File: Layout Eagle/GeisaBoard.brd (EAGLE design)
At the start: 100 x 80 mm, 20 parts, among them IC1 4052N, IC2 4052N, U1 328P

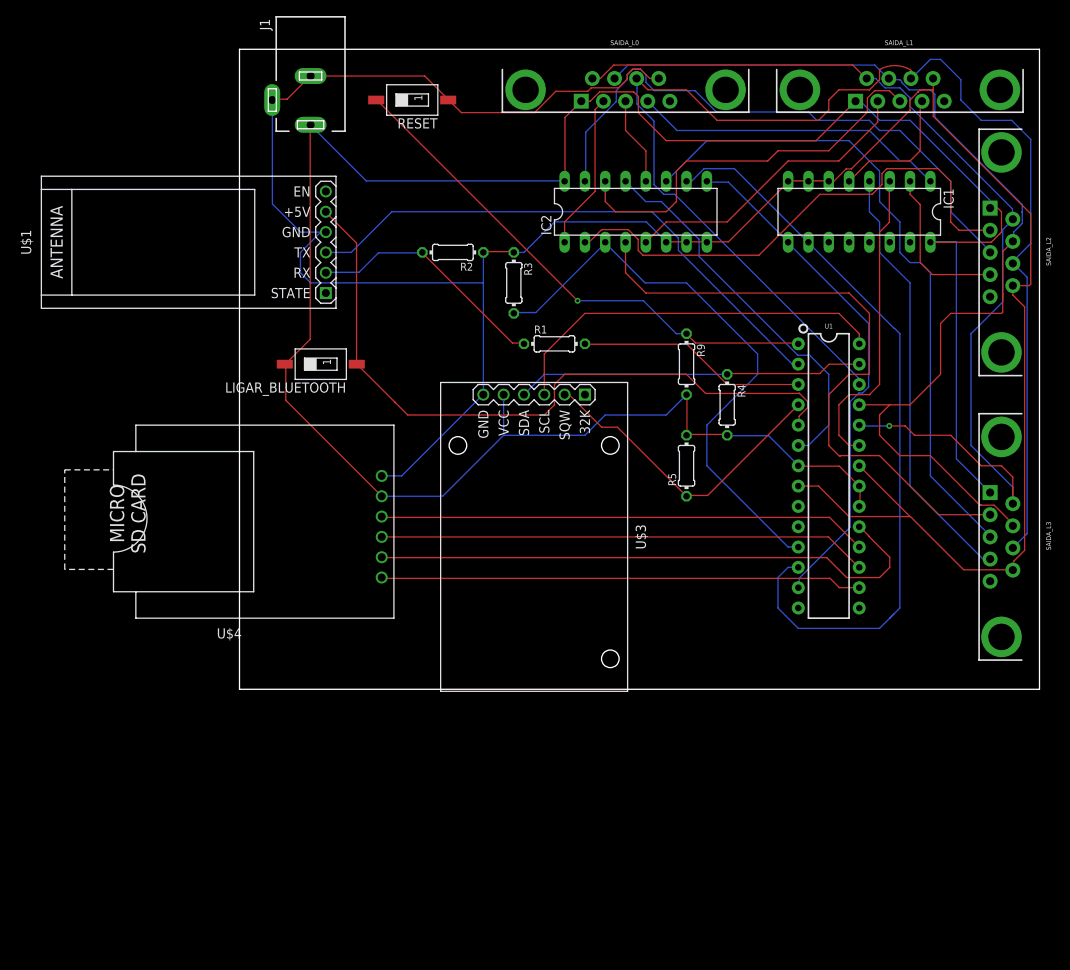
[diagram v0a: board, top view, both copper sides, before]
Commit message: Layout com correção inicial do Padrão
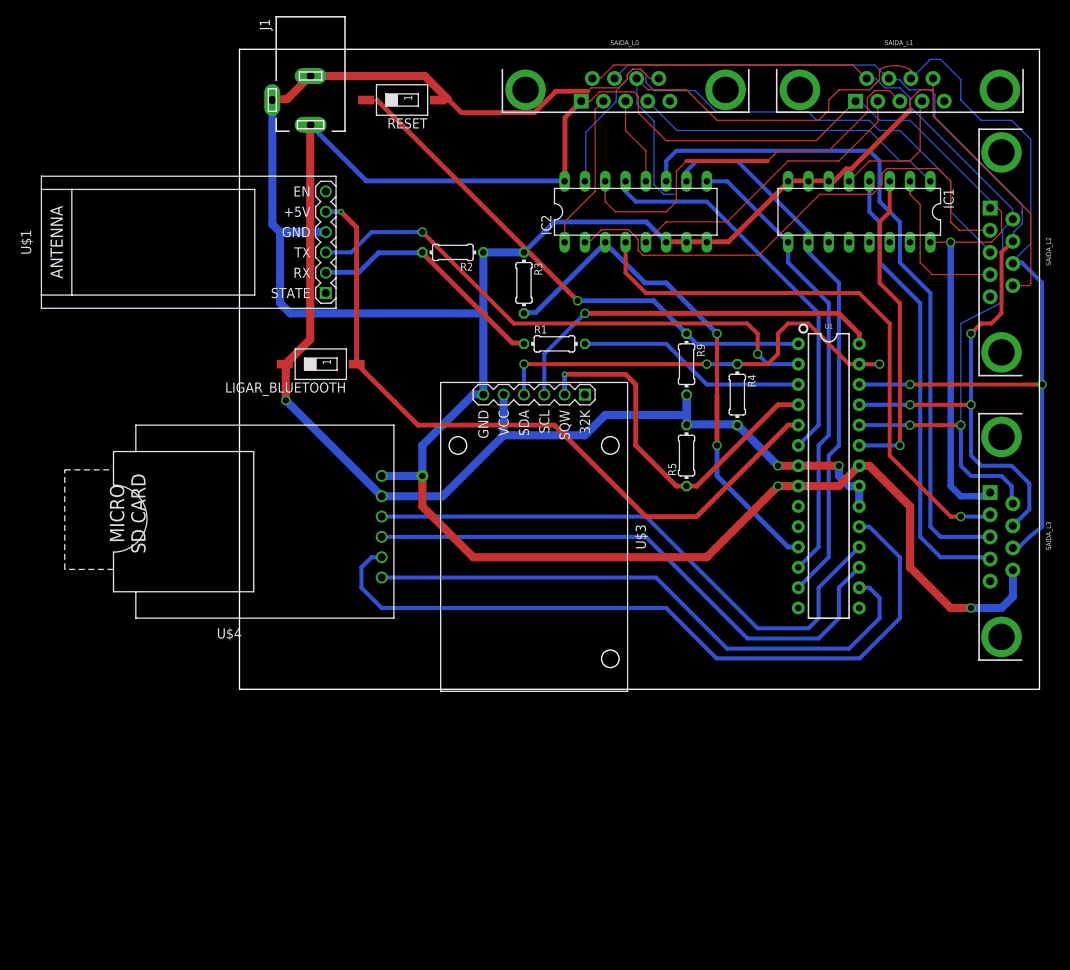
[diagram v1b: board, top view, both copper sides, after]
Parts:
- moved R4 1.80 mm to (62.2, 36.8)
- moved R3 1.27 mm to (35.6, 50.8)
- moved R5 1.27 mm to (55.9, 29.2)
- moved RESET 1.27 mm to (20.3, 73.7)
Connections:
- net S0: now also U1.13; no longer U1.12
- net S1: now also U1.12; no longer U1.13
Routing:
- net GND: track 320.0 -> 356.8 mm, vias 0 -> 3
- net S0: track 95.2 -> 68.9 mm
- net SPI_SCK: track 71.8 -> 92.9 mm
- net SS_SD: track 60.4 -> 73.2 mm
- net RTC_SDA: track 43.7 -> 56.5 mm, vias 0 -> 4
- net SPI_MISO: track 61.3 -> 71.9 mm
- net SPI_MOSI: track 61.3 -> 70.9 mm
- net DO_ADC: track 127.7 -> 119.4 mm, vias 1 -> 2
- net ATIVA3: track 81.1 -> 72.8 mm, vias 0 -> 1
- net LEIRASATIVAS: track 72.3 -> 64.2 mm, vias 0 -> 2
- net RTC_SQW: track 39.2 -> 46.2 mm, vias 0 -> 1
- net S1: track 64.6 -> 57.6 mm
- net CLK_ADC: track 167.5 -> 160.6 mm, vias 0 -> 2
- net VCC: track 292.9 -> 299.0 mm, vias 0 -> 6
- net TEMP3: track 83.2 -> 87.4 mm
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
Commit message: Novo layout feito com melhores definições de espessura de trilhas e outros parâmetros
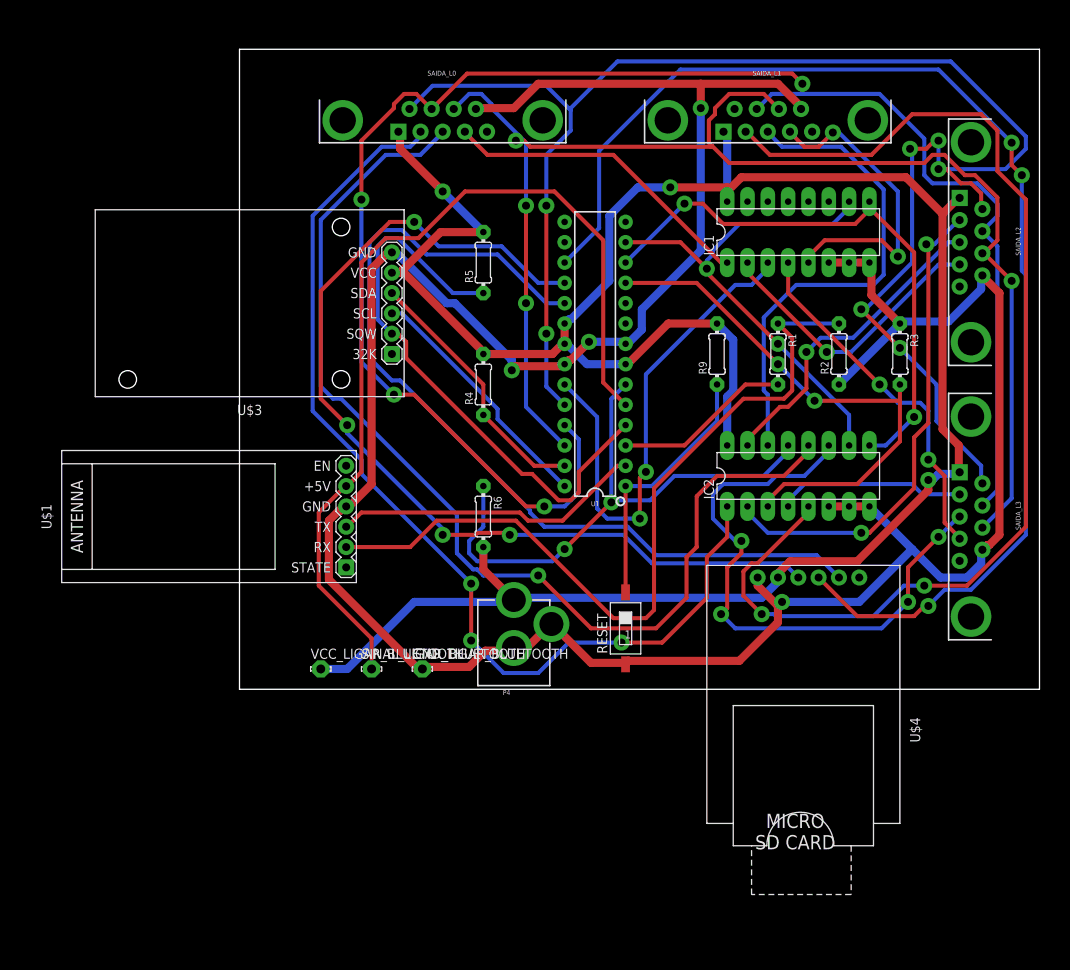
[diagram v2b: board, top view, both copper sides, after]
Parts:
- removed J1: (no value), con-jack:DCJ0303
- removed LIGAR_BLUETOOTH: SWS001, smd-special:SMS-001
- added GND_LIGAR_BLUETOOTH, SINAL_LIGAR_BLUETOOTH, VCC_LIGAR_BLUETOOTH: LSP11, solpad:LSP11
- added P4: POWER_JACK, SparkFun-Connectors:POWER_JACK_PTH
- added R6: 4k7, rcl:0204/7
- moved FRAME1 166.6 mm to (-80.0, 124.5)
- moved RESET 71.7 mm to (48.3, 7.62), turned to 0 degrees
- moved U$4 68.1 mm to (72.4, 2.54), turned to 270 degrees
- moved R2 49.9 mm to (74.9, 41.9), turned to 90 degrees
- moved R3 47.8 mm to (82.5, 41.9)
- moved U$3 46.0 mm to (1.27, 48.3), turned to 180 degrees
- moved IC2 38.8 mm to (69.8, 26.7)
- moved R5 35.0 mm to (30.5, 53.3)
- moved U$1 34.4 mm to (-3.81, 21.6)
- moved U1 32.9 mm to (44.5, 41.9), turned to 90 degrees
- moved R4 31.8 mm to (30.5, 38.1), turned to 90 degrees
- moved R1 28.0 mm to (67.3, 41.9), turned to 270 degrees
- moved SAIDA_L0 23.2 mm to (25.4, 71.1)
- moved SAIDA_L1 16.9 mm to (66.0, 71.1)
- moved IC1 8.03 mm to (69.8, 57.1), turned to 0 degrees
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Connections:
- net BLUETOOTH_LIGADO: now also SINAL_LIGAR_BLUETOOTH.MP; no longer LIGAR_BLUETOOTH.1
- net GND: now also GND_LIGAR_BLUETOOTH.MP, P4.GND, P4.GNDBREAK; no longer J1.2, J1.3
- net TEMPERATURA: now also R6.1
- net VCC: now also P4.PWR, R6.2, VCC_LIGAR_BLUETOOTH.MP; no longer J1.1, LIGAR_BLUETOOTH.2
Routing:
- net TEMP0: track 11.1 -> 133.6 mm, vias 0 -> 1
- net ATIVA0: track 19.6 -> 127.0 mm, vias 0 -> 3
- net ATIVA1: track 37.8 -> 142.6 mm, vias 0 -> 2
- net DI_ADC: track 124.4 -> 213.7 mm, vias 3 -> 4
- net DO_ADC: track 119.4 -> 205.8 mm, vias 2 -> 7
- net SPI_MOSI: track 70.9 -> 157.2 mm, vias 0 -> 3
- net SS_SD: track 73.2 -> 0.00 mm
- net 3,3_BT_R: track 30.6 -> 99.6 mm
- net ATIVA3: track 72.8 -> 23.6 mm, vias 1 -> 0
- net SPI_MISO: track 71.9 -> 120.9 mm, vias 0 -> 4
- net N$12: track 66.7 -> 32.7 mm, vias 1 -> 0
- net TEMP2: track 73.6 -> 40.2 mm, vias 0 -> 1
- net ATM_R_BT_T: track 68.5 -> 38.9 mm, vias 2 -> 0
- net RTC_SQW: track 46.2 -> 72.5 mm, vias 1 -> 0
- net BLUETOOTH_LIGADO: track 89.9 -> 114.1 mm, vias 1 -> 0
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
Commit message: Layout
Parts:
- moved R2 44.8 mm to (31.2, 32.0)
- moved P4 44.5 mm to (78.7, -3.81)
- moved IC2 42.1 mm to (36.3, 52.1), turned to 270 degrees
- moved GND_LIGAR_BLUETOOTH 36.9 mm to (13.0, 38.1)
- moved VCC_LIGAR_BLUETOOTH 35.9 mm to (7.11, 38.4)
- moved R6 35.3 mm to (56.9, 45.0)
- moved SINAL_LIGAR_BLUETOOTH 34.1 mm to (18.3, 36.6)
- moved R5 33.8 mm to (30.2, 19.6), turned to 270 degrees
- moved R9 31.4 mm to (81.3, 19.1), flipped to the bottom, turned to 270 degrees
- moved U$1 30.7 mm to (3.05, 51.6)
- moved R4 28.2 mm to (37.1, 10.7), turned to 270 degrees
- moved R3 27.2 mm to (56.6, 33.8), turned to 180 degrees
- moved R1 25.6 mm to (42.7, 35.1), turned to 0 degrees
- moved U$3 25.4 mm to (2.03, 22.9)
- moved RESET 21.4 mm to (69.6, 8.64)
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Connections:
- net N$12 renamed RESET/
- net GND: now also SAIDA_L0.5, SAIDA_L1.5, SAIDA_L2.5, SAIDA_L3.5; no longer SAIDA_L0.9, SAIDA_L1.9, SAIDA_L2.9, SAIDA_L3.9
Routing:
- net GND: track 356.8 -> 43.5 mm, vias 4 -> 5
- net VCC: track 306.5 -> 29.1 mm, vias 3 -> 5
- net SPI_MOSI: track 157.2 -> 29.7 mm, vias 3 -> 0
- net ATIVA0: track 127.0 -> 17.4 mm, vias 3 -> 0
- net SPI_MISO: track 120.9 -> 17.2 mm, vias 4 -> 0
- net TEMP0: track 133.6 -> 30.8 mm, vias 1 -> 0
- net SPI_SCK: track 113.5 -> 18.2 mm
- net ATIVA3: track 23.6 -> 113.4 mm, vias 0 -> 1
- net ATIVA1: track 142.6 -> 65.4 mm, vias 2 -> 1
- net 3,3_BT_R: track 99.6 -> 27.2 mm
- net BLUETOOTH_LIGADO: track 114.1 -> 70.2 mm
- net SS_ADC0: track 39.6 -> 80.9 mm, vias 0 -> 1
- net SS_SD: track 0.00 -> 38.8 mm
- net RTC_SCL: track 31.3 -> 69.4 mm
- net TEMPERATURA: track 71.2 -> 41.1 mm, vias 2 -> 0
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- added copper zone on layer 1, net GND
- added copper zone on layer 16, net VCC
